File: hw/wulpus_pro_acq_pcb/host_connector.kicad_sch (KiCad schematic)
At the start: 18 parts, among them J12 DF40HC(3.0)-50DS-0.4V(51), J13 Solder Jumper, U17 SN74AVC4T774RSVR, U18 SN74AVC4T774RSVR, X1 68000-106HLF, X3 68000-106HLF, X4 68000-106HLF, X5 68000-102HLF, X6 68000-102HLF, X7 68000-102HLF, X8 68000-102HLF

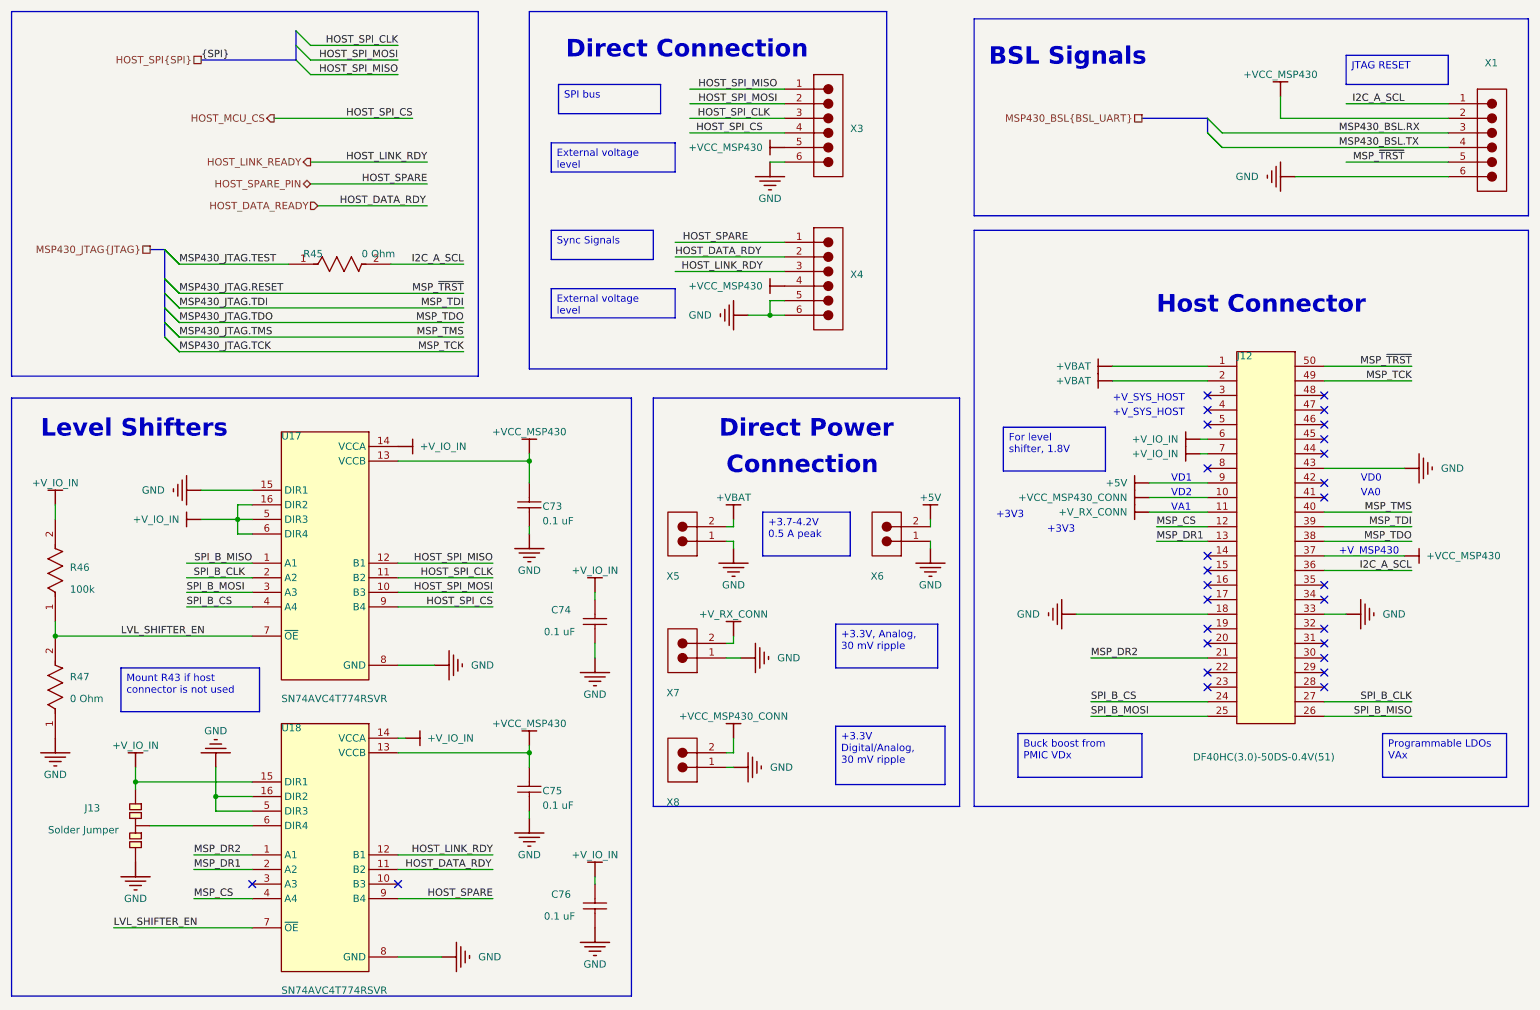
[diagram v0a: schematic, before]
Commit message: Cleaned teh project, removen eval board components
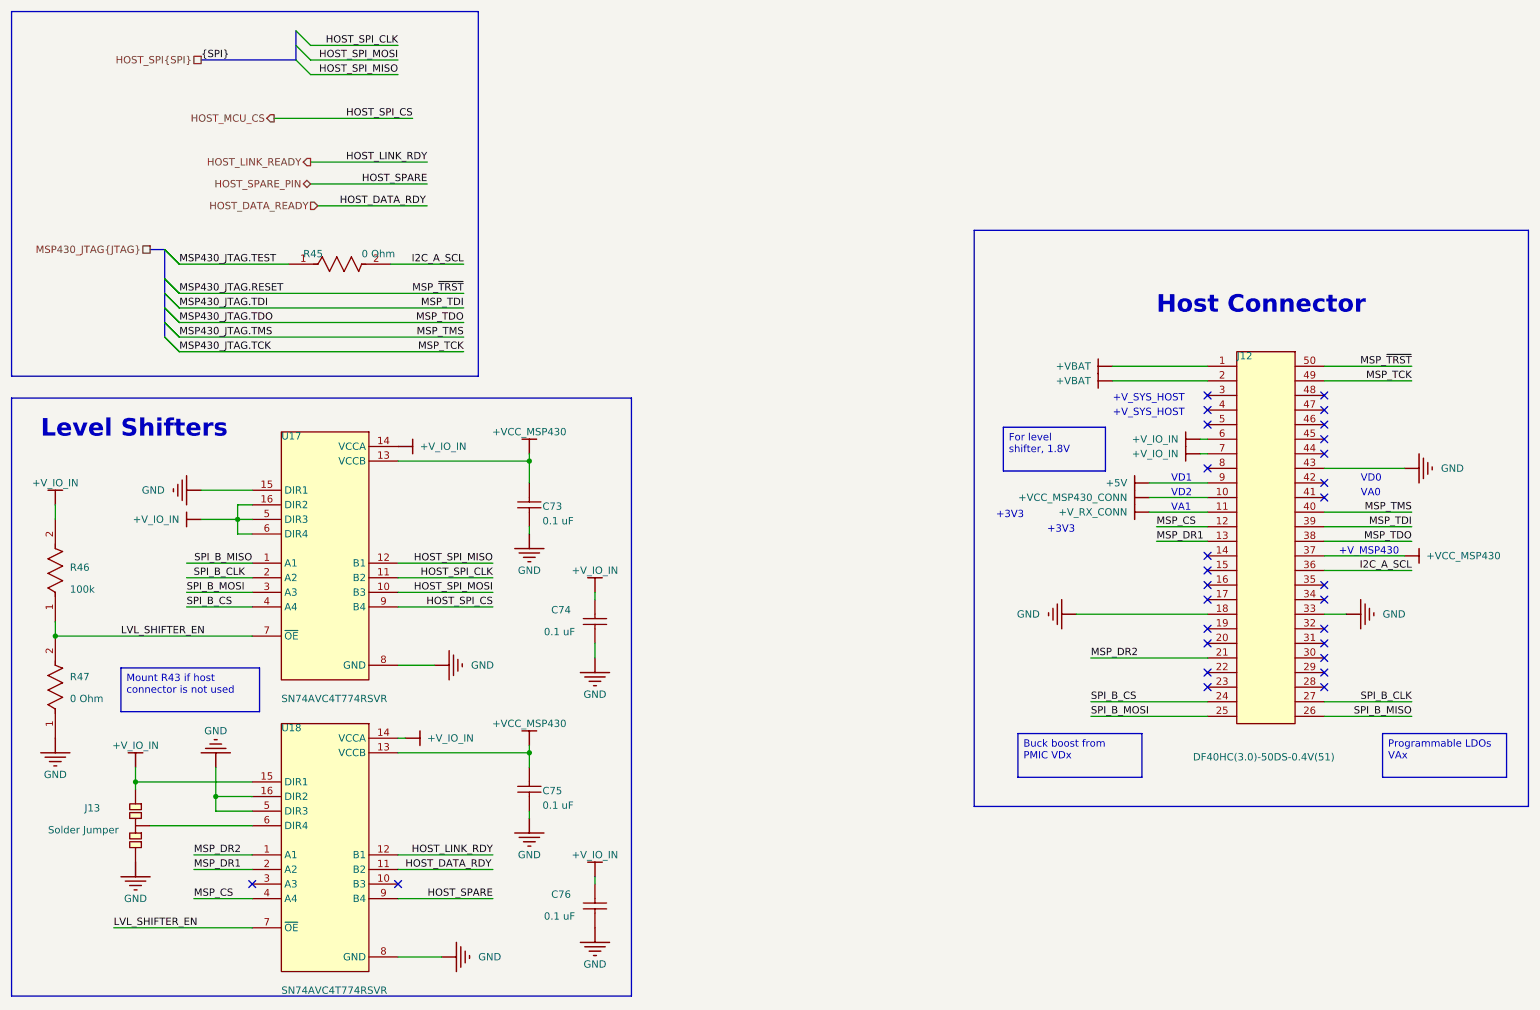
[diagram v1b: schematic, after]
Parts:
- removed X1, X3, X4: 68000-106HLF, 68000-106HLF, symbol ETHZ Vault:U_host_connector_3_CON-1x6-Male_ETHZ Vault
- removed X5, X6, X7, X8: 68000-102HLF, 68000-102HLF, symbol ETHZ Vault:U_host_connector_1_CON-1x2-Male_ETHZ Vault
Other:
- note removed: "BSL Signals"
- note removed: "Connection"
- note removed: "Direct Connection"
- note removed: "Direct Power"
